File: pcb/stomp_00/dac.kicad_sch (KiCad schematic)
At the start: 14 parts, among them J4 Headphones, U11 AP7313-18SAG, U9 SGTL5000XNAA3

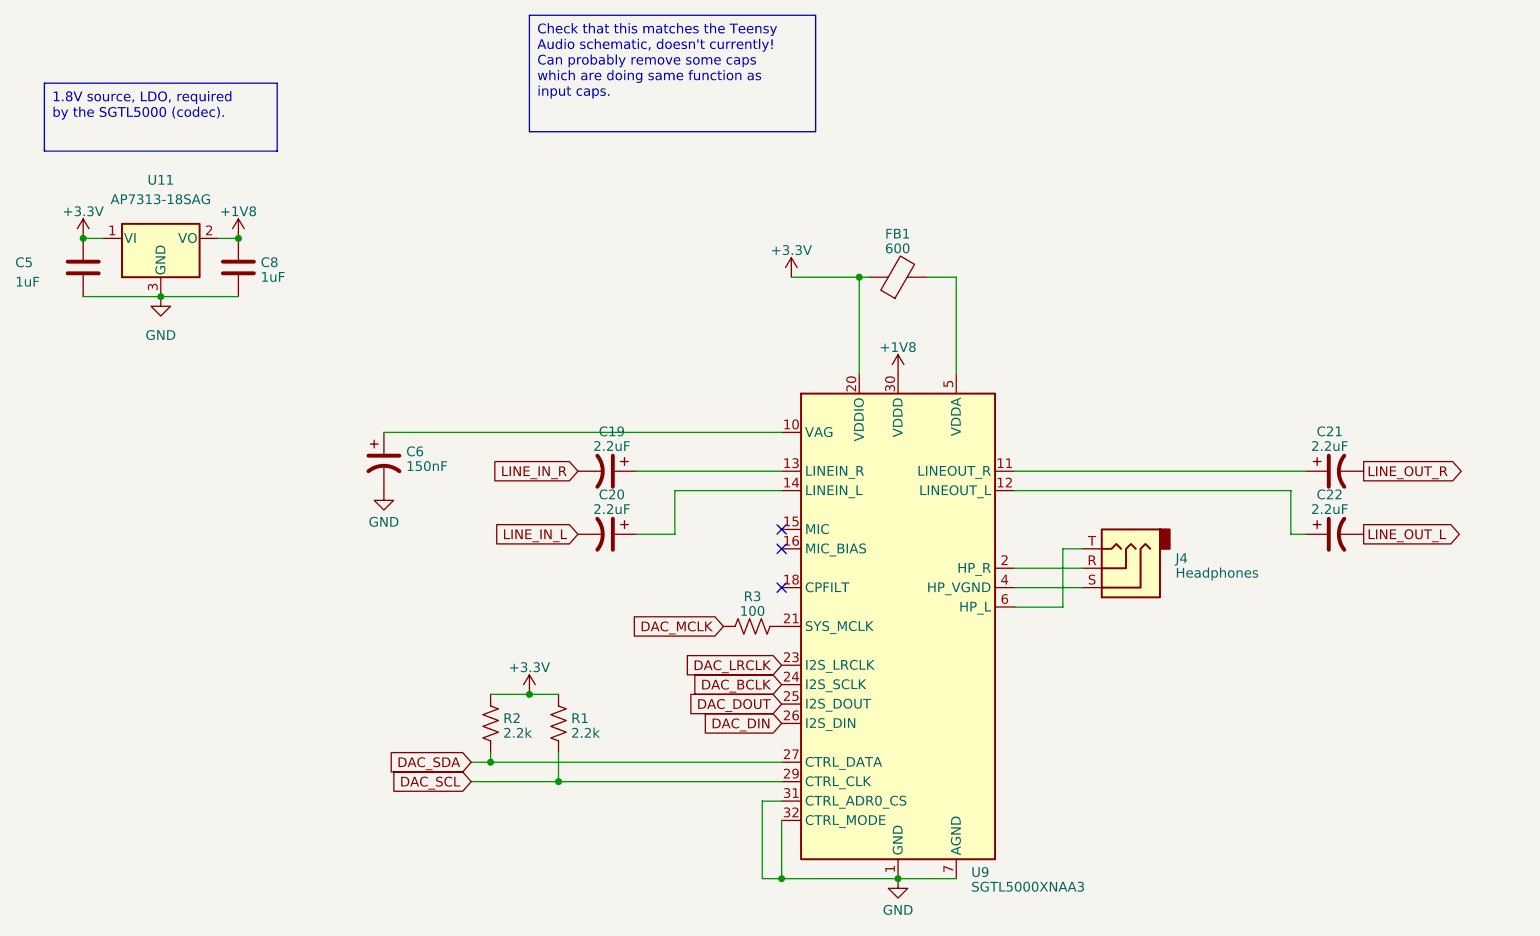
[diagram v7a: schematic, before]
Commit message: tidying up dac connections
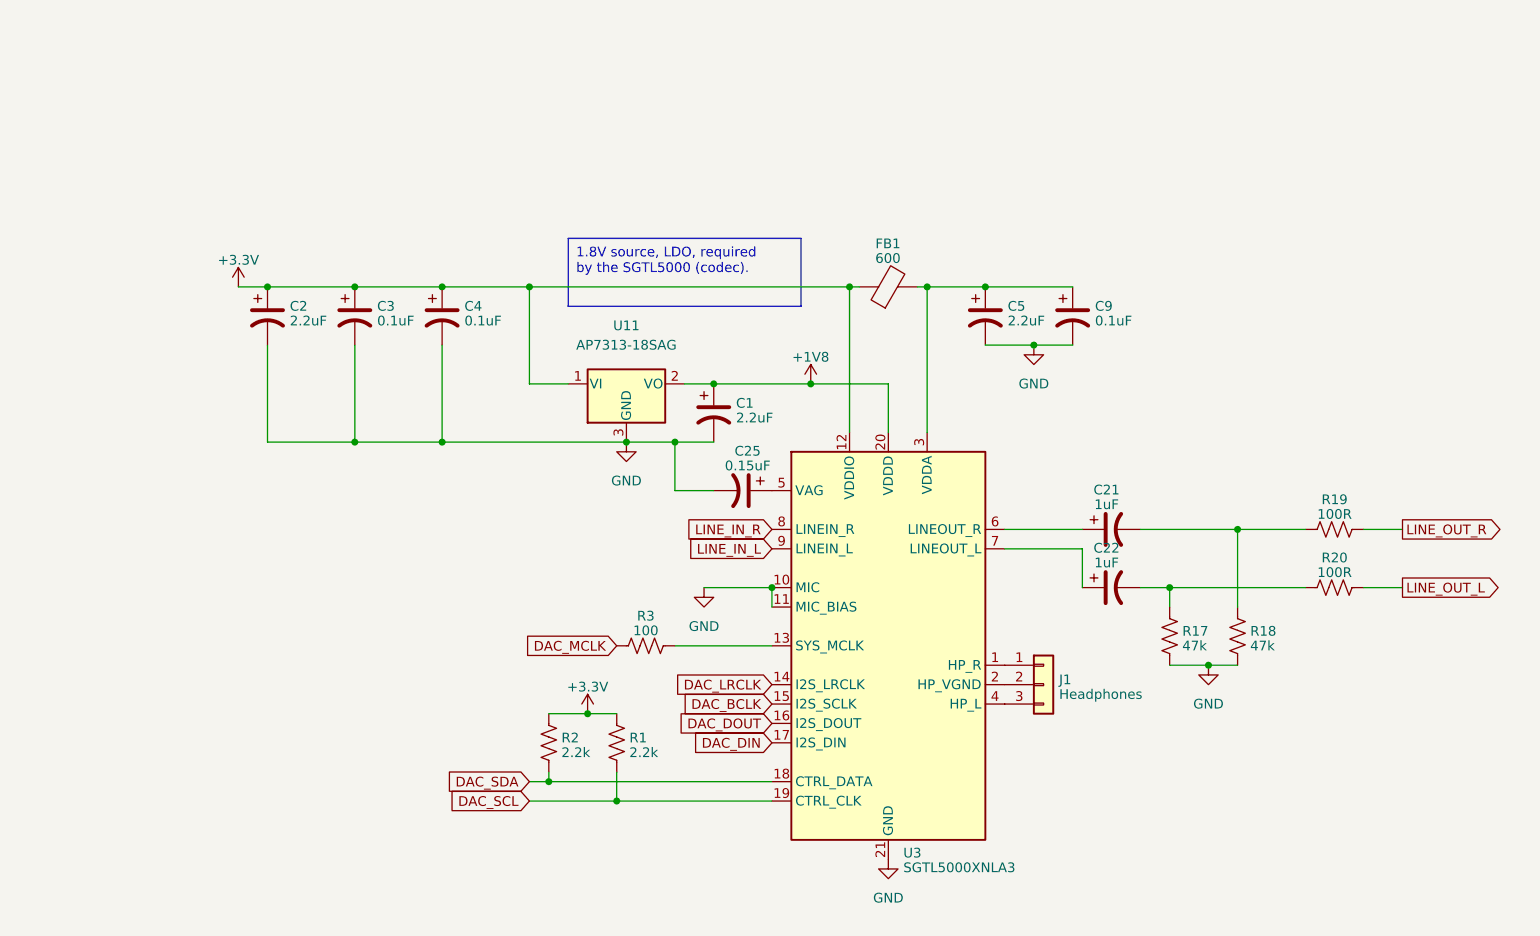
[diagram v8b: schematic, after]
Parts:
- removed C19, C20: 2.2uF, symbol Device:C_Polarized_US
- removed C5, C8: 1uF, Capacitor_SMD:C_0603_1608Metric, symbol Device:C
- removed C6: 150nF, symbol Device:C_Polarized_US
- removed J4: Headphones, Connector_PinHeader_2.54mm:PinHeader_1x03_P2.54mm_Vertical, symbol Connector_Audio:AudioJack3
- removed U9: SGTL5000XNAA3, Package_DFN_QFN:QFN-32-1EP_5x5mm_P0.5mm_EP3.6x3.6mm, symbol Audio:SGTL5000XNAA3
- added C1, C2, C5: 2.2uF, Capacitor_SMD:C_0603_1608Metric, symbol Device:C_Polarized_US
- added C25: 0.15uF, Capacitor_SMD:C_0603_1608Metric, symbol Device:C_Polarized_US
- added C3, C4, C9: 0.1uF, Capacitor_SMD:C_0603_1608Metric, symbol Device:C_Polarized_US
- added J1: Headphones, Connector_PinHeader_2.54mm:PinHeader_1x03_P2.54mm_Vertical, symbol Connector_Generic:Conn_01x03
- added R17, R18: 47k, Resistor_SMD:R_0603_1608Metric, symbol Device:R_US
- added R19, R20: 100R, Resistor_SMD:R_0603_1608Metric, symbol Device:R_US
- added U3: SGTL5000XNLA3, Package_DFN_QFN:QFN-20-1EP_3x3mm_P0.4mm_EP1.65x1.65mm, symbol Audio:SGTL5000XNLA3
- C21, C22: value 2.2uF -> 1uF; footprint (none) -> Capacitor_SMD:C_0603_1608Metric
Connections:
- net +1V8: now also C1.1, U3.20 (VDDD)
- net +3.3V: now also C2.1, C3.1, C4.1, U3.12 (VDDIO)
- net DAC_BCLK: now also U3.15 (I2S_SCLK)
- net DAC_DIN: now also U3.17 (I2S_DIN)
- net DAC_DOUT: now also U3.16 (I2S_DOUT)
- net DAC_LRCLK: now also U3.14 (I2S_LRCLK)
- net DAC_SCL: now also U3.19 (CTRL_CLK)
- net DAC_SDA: now also U3.18 (CTRL_DATA)
- net GND: now also C1.2, C2.2, C25.2, C3.2, C4.2, C5.2, C9.2, R17.1, R18.1, U3.10 (MIC), U3.11 (MIC_BIAS), U3.21 (GND)
- net LINE_IN_L: now also U3.9 (LINEIN_L)
- net LINE_IN_R: now also U3.8 (LINEIN_R)
- net LINE_OUT_L: now also R20.1; no longer C22.2
- net LINE_OUT_R: now also R19.1; no longer C21.2
- net at FB1.2: now also C5.1, C9.1, U3.3 (VDDA)
- net at C21.1: now also U3.6 (LINEOUT_R)
- net at C22.1: now also U3.7 (LINEOUT_L)
- net at R3.1: now also U3.13 (SYS_MCLK)
- new net: C25.1, U3.5 (VAG)
- new net: C22.2, R17.2, R20.2
- new net: C21.2, R18.2, R19.2
- new net: J1.1 (Pin_1), U3.1 (HP_R)
- new net: J1.2 (Pin_2), U3.2 (HP_VGND)
- new net: J1.3 (Pin_3), U3.4 (HP_L)
- no-connect marks 3 -> 0
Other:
- moved on the sheet: C21, C22, FB1, R1, R2, R3, U11
